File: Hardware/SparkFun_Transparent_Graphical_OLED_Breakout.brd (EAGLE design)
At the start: 25.4 x 25.4 mm, 66 parts, among them U1 AP3012, U2 UG-2856KLBAG01_4WSPI

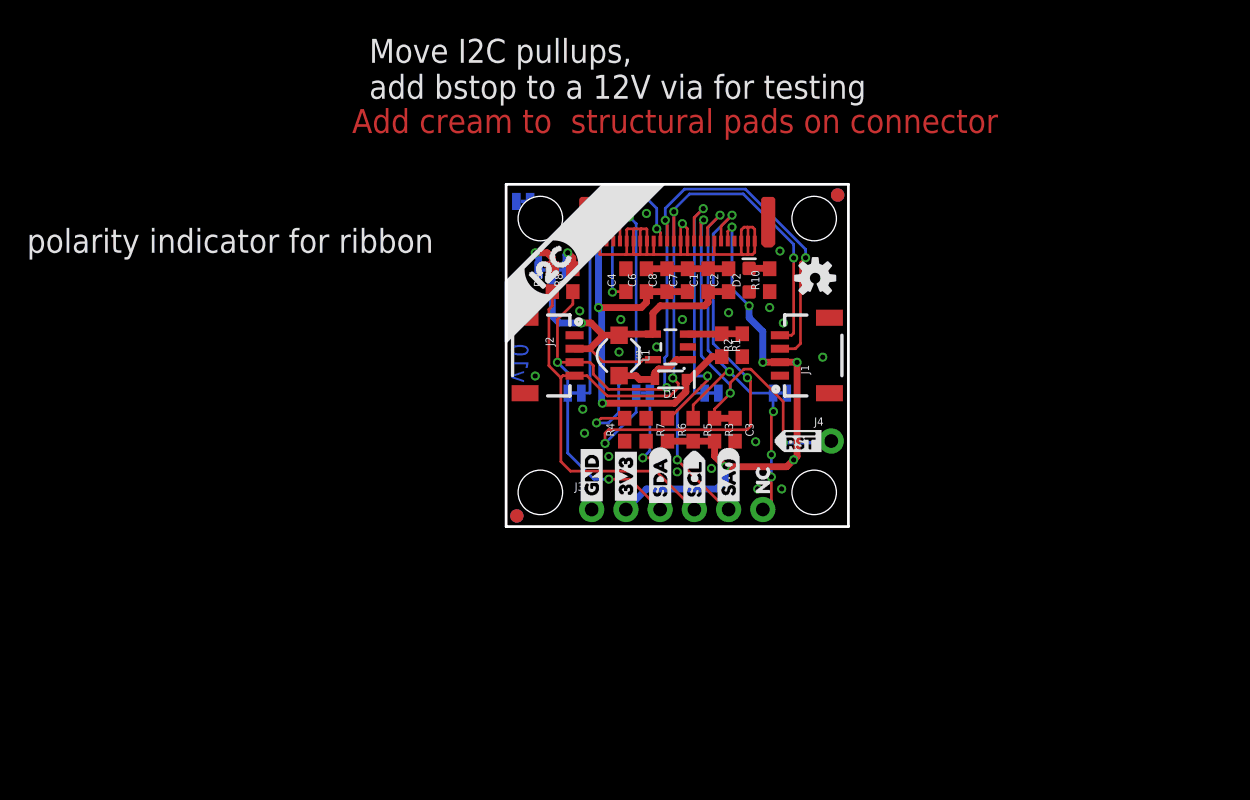
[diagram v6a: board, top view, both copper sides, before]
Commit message: Fixed design review notes
Jumper labels simplified
FPC polarity markers added
version number updated
I2C resistors moved
test point added for 12V
LED disconnect jumper added
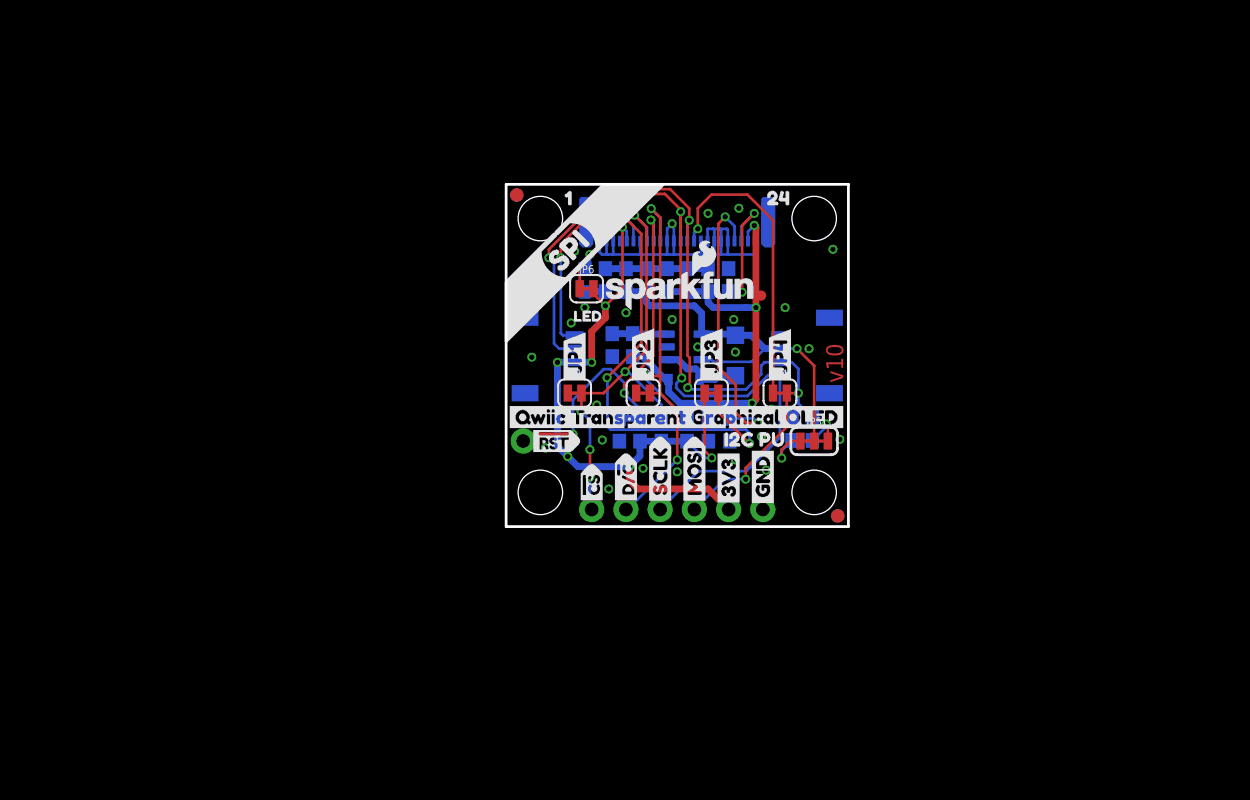
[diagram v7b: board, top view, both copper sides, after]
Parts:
- removed U$26: (no value), buzzard_labels:IFS17
- added H1, H2, H3, H4: STAND-OFF, SparkFun-Hardware:STAND-OFF
- added TP1: 12V, SparkFun-Connectors:PAD.03X.03
- J1, J2: device SparkFun-Connectors:1X04_1MM_RA -> SparkFun-Connectors:JST04_1MM_RA
- JP6: value PWR -> LED
- U$1: value QWIIC_BOARD_OUTLINEH -> (none); device SparkX:QWIIC_BOARD_MOUNT_HOLES -> buzzard_labels:JP10
- U$11: device buzzard_labels:I2C13 -> buzzard_labels:JP32
- U$16: device buzzard_labels:GND10 -> buzzard_labels:JP43
- U$18: device buzzard_labels:013 -> buzzard_labels:LED4
- U$21: device buzzard_labels_1:SA05 -> buzzard_labels:PWR5
- U$22: device buzzard_labels:I2C13 -> buzzard_labels:17
- U$23: device buzzard_labels_1:#CS4 -> buzzard_labels:248
- U$3: device buzzard_labels_1:D27 -> buzzard_labels:JP21
- moved FRAME1 48.3 mm to (36.8, -10.2), flipped to the bottom
- moved U$2 25.9 mm to (-0.25, 8.13), flipped to the top
- moved FD1 23.8 mm to (24.6, 0.79), flipped to the bottom
- moved FD2 23.8 mm to (24.6, 0.79), flipped to the top
- moved FD3 23.8 mm to (0.79, 24.6), flipped to the bottom
- moved FD4 23.8 mm to (0.79, 24.6), flipped to the top
- moved JP5 23.2 mm to (22.9, 6.35), flipped to the top, turned to 0 degrees
- moved U$19 23.1 mm to (24.3, 17.1), flipped to the bottom
- moved J4 22.9 mm to (1.27, 6.35), flipped to the bottom
- moved U$17 22.7 mm to (1.37, 6.35), flipped to the top
- moved U$24 21.6 mm to (2.54, 18.4), flipped to the top
- moved LOGO2 21.0 mm to (1.91, 18.2), flipped to the bottom
- moved R8 20.9 mm to (22.7, 7.24), flipped to the bottom, turned to 270 degrees
- moved R9 20.9 mm to (21.2, 7.24), flipped to the bottom, turned to 270 degrees
- moved J1 15.2 mm to (5.08, 12.7), flipped to the bottom
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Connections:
- net 12V: now also TP1.P$1
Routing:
- net SCLK/SCL: track 68.3 -> 59.4 mm
- net N$8: track 0.00 -> 4.04 mm, vias 0 -> 1
- net SDIN/SDA: track 67.5 -> 63.8 mm
- net 3.3V: track 77.2 -> 79.3 mm
- net GND: track 41.5 -> 43.0 mm, vias 23 -> 27
- net N$6: track 2.66 -> 3.39 mm
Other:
- board text removed: "Add cream to structural pads on connector"
- board text removed: "Jumper labels fix (simplify)"
- board text removed: "Move I2C pullups, add bstop to a 12V via for testing"
- board text removed: "Use JP4, JP3, JP2, JP1"
- board text removed: "Version number update"
- board text removed: "polarity indicator for ribbon"

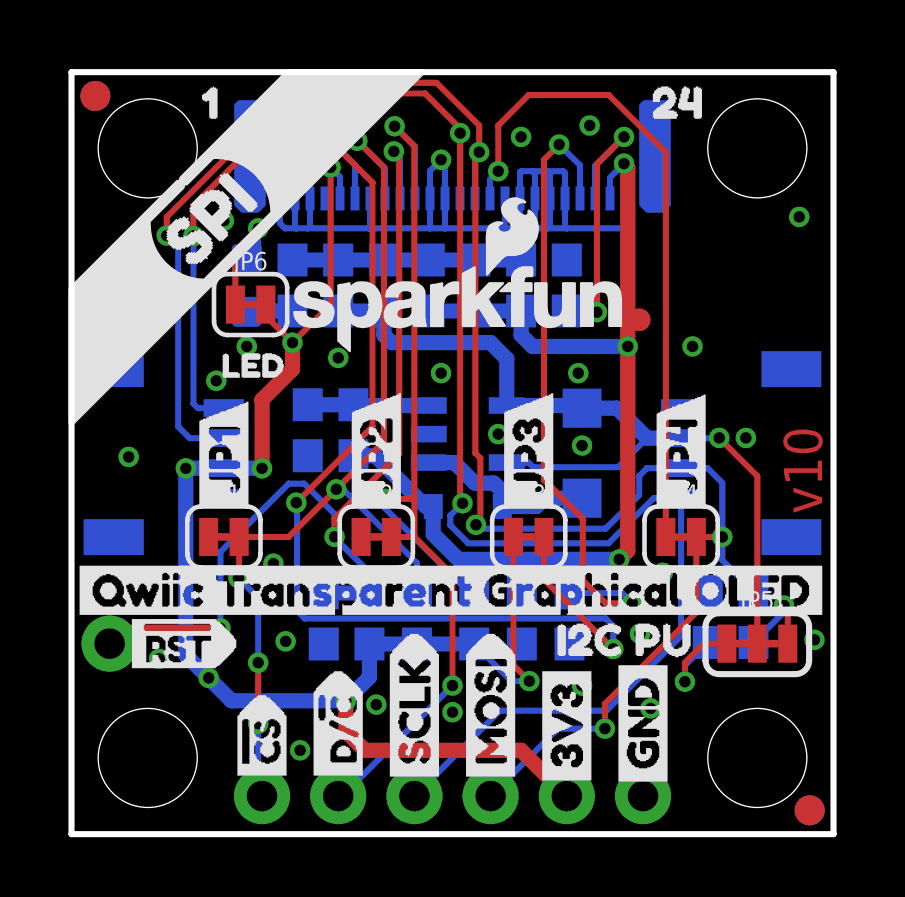
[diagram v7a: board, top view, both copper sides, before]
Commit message: Minor changes from Checklist run-through
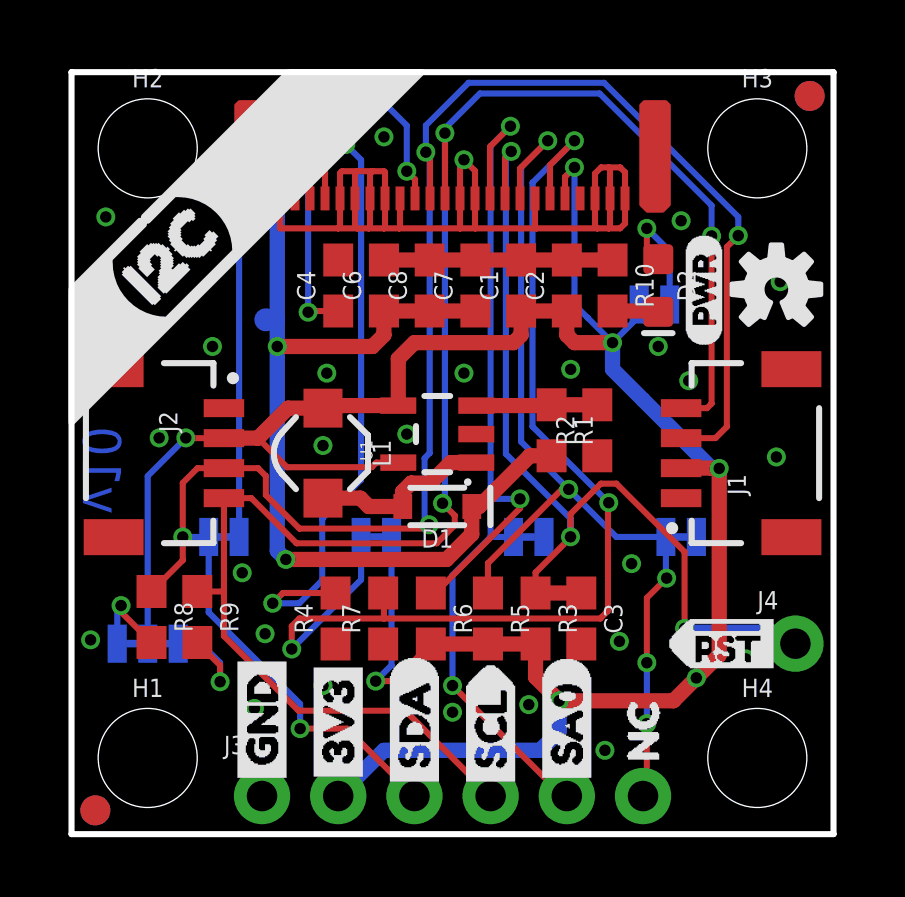
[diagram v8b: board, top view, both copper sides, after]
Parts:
- moved FRAME1 48.3 mm to (-11.4, -10.2), flipped to the top
- moved U$2 25.9 mm to (25.7, 8.13), flipped to the bottom
- moved FD1 23.8 mm to (0.79, 0.79), flipped to the top
- moved FD2 23.8 mm to (0.79, 0.79), flipped to the bottom
- moved FD3 23.8 mm to (24.6, 24.6), flipped to the top
- moved FD4 23.8 mm to (24.6, 24.6), flipped to the bottom
- moved U$19 23.1 mm to (1.14, 17.1), flipped to the top
- moved J4 22.9 mm to (24.1, 6.35), flipped to the top
- moved U$17 22.7 mm to (24.0, 6.35), flipped to the bottom
- moved LOGO2 21.6 mm to (23.5, 18.2), flipped to the top
- moved H1 20.3 mm to (2.54, 2.54), flipped to the top
- moved H2 20.3 mm to (2.54, 22.9), flipped to the top
- moved H3 20.3 mm to (22.9, 22.9), flipped to the top
- moved H4 20.3 mm to (22.9, 2.54), flipped to the top
- moved JP5 20.3 mm to (2.54, 6.35), flipped to the bottom
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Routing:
- net 3.3V: track 79.3 -> 81.6 mm, vias 8 -> 7
- net !4WSPI!/I2C: track 35.8 -> 36.6 mm
